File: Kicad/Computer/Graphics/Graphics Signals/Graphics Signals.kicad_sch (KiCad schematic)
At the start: 26 parts, among them IC1 74LVC1G04GV,125, IC10 74LVC74APW,118, IC11 74LVC32APW,118, IC2 74LVC74APW,118, IC2 AP7365-33WG-7, IC3 74LVC74APW,118, IC4 SN74LVC1G332DCKR, IC6 74LVC125APW-Q100J, IC9 74LVC1GX04GW,125, J7 Conn_02x16_Counter_Clockwise

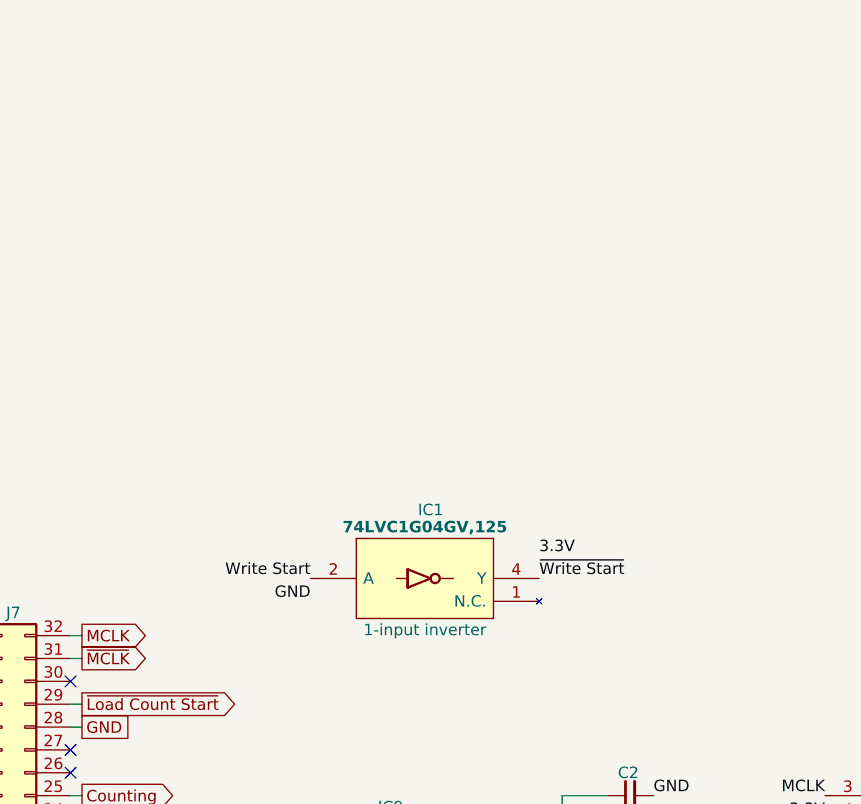
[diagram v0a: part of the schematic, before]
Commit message: Added a Blitter Board.
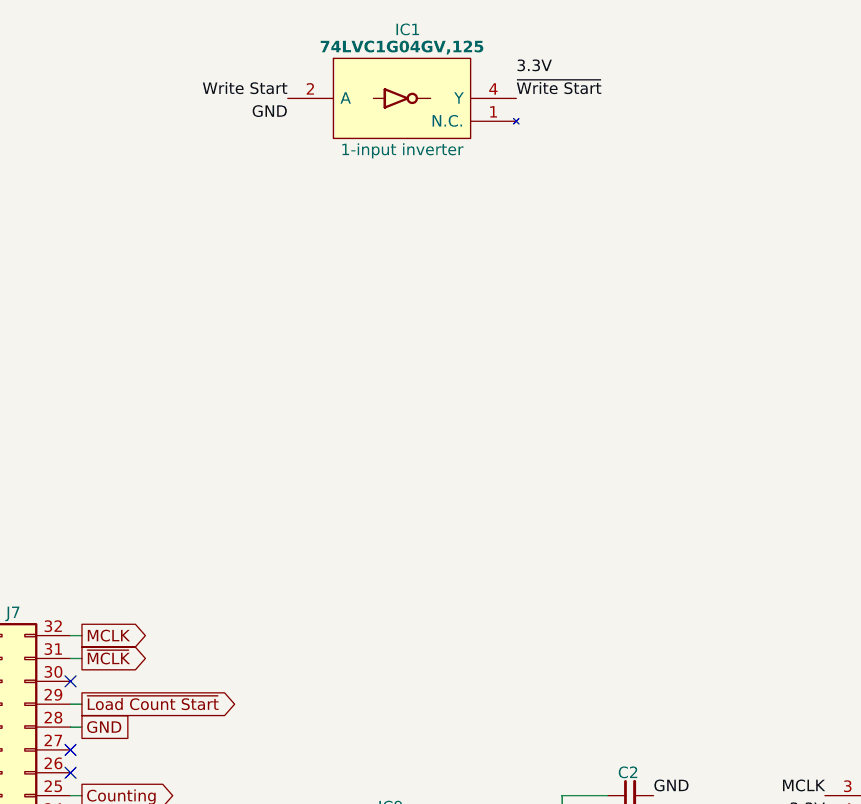
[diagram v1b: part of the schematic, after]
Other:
- moved on the sheet: IC1
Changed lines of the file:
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@@
 	)
 	(label "~{Write Start}"
-		(at 97.79 81.28 0)
+		(at 95.25 27.94 0)
 		(fields_autoplaced yes)
 		(effects
@@
 	)
 	(label "GND"
-		(at 72.39 83.82 180)
+		(at 69.85 30.48 180)
 		(fields_autoplaced yes)
 		(effects
@@
 	)
 	(label "Write Start"
-		(at 72.39 81.28 180)
+		(at 69.85 27.94 180)
 		(fields_autoplaced yes)
 		(effects
@@
 	)
 	(label "3.3V"
-		(at 97.79 78.74 0)
+		(at 95.25 25.4 0)
 		(fields_autoplaced yes)
 		(effects
@@
 	(symbol
 		(lib_id "Nexperia:74LVC1G04GV,125")
-		(at 72.39 78.74 0)
+		(at 69.85 25.4 0)
 		(unit 1)
 		(exclude_from_sim no)
@@
 		(dnp no)
 		(property "Reference" "IC1"
-			(at 85.725 73.66 0)
+			(at 83.185 20.32 0)
 			(effects
 				(font
@@
 		)
 		(property "Value" "74LVC1G04GV,125"
-			(at 85.09 75.565 0)
+			(at 82.55 22.225 0)
 			(effects
 				(font
@@
 		)
 		(property "Footprint" "SamacSys_Parts:SOT95P275X110-5N"
-			(at 98.425 101.6 0)
+			(at 95.885 48.26 0)
 			(effects
 				(font
@@
 		)
 		(property "Datasheet" "https://assets.nexperia.com/documents/data-sheet/74LVC1G04.pdf"
-			(at 98.425 104.14 0)
+			(at 95.885 50.8 0)
 			(effects
 				(font
@@
 		)
 		(property "Description" "1-input inverter"
-			(at 85.09 86.995 0)
+			(at 82.55 33.655 0)
 			(effects
 				(font
@@
 		)
 		(property "Height" "1.1"
-			(at 98.425 109.22 0)
+			(at 95.885 55.88 0)
 			(effects
 				(font
@@
 		)
 		(property "Manufacturer_Name" "Nexperia"
-			(at 98.425 111.76 0)
+			(at 95.885 58.42 0)
 			(effects
 				(font
@@
 		)
 		(property "Manufacturer_Part_Number" "74LVC1G04GV,125"
-			(at 98.425 114.3 0)
+			(at 95.885 60.96 0)
 			(effects
 				(font
@@
 		)
 		(property "Mouser Part Number" "771-74LVC1G04GV"
-			(at 98.425 116.84 0)
+			(at 95.885 63.5 0)
 			(effects
 				(font
@@
 		)
 		(property "Mouser Price/Stock" "https://www.mouser.co.uk/ProductDetail/Nexperia/74LVC1G04GV125?qs=me8TqzrmIYW6McwMAxl%2F9w%3D%3D"
-			(at 98.425 119.38 0)
+			(at 95.885 66.04 0)
 			(effects
 				(font
@@
 		)
 		(property "Silkscreen" "'1G04"
-			(at 85.725 89.535 0)
-			(effects
-				(font
+			(at 83.185 36.195 0)
+			(effects
+				(font

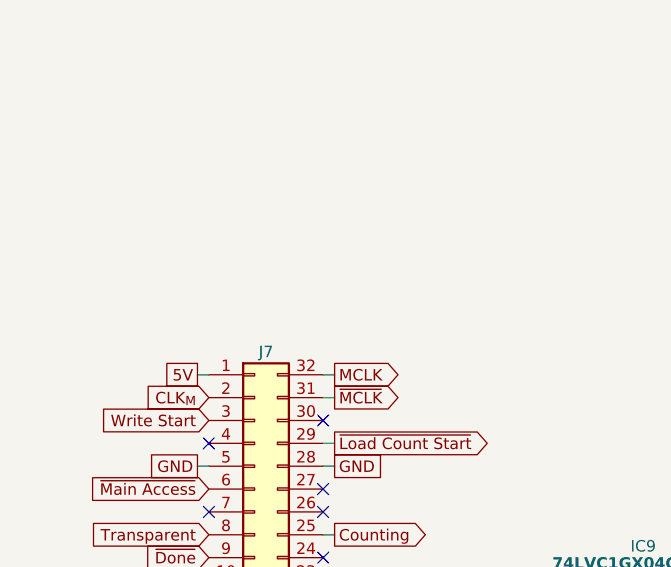
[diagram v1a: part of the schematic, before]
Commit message: Use VRML instead of STEPs for Processor Board models.
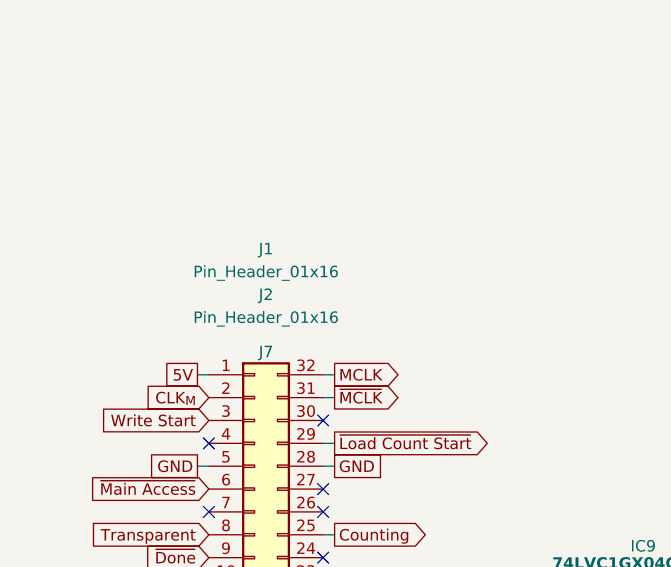
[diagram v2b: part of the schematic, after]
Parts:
- added J1, J2: Pin_Header_01x16, SamacSys_Parts:PinHeader_1x16_P2.54mm_Vertical, symbol HCP65:Pin_Header_01x32
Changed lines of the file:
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@@
+	)
+	(symbol
+		(lib_id "HCP65:Pin_Header_01x32")
+		(at 39.37 74.93 0)
+		(mirror y)
+		(unit 1)
+		(exclude_from_sim no)
+		(in_bom yes)
+		(on_board yes)
+		(dnp no)
+		(property "Reference" "J1"
+			(at 39.37 73.66 0)
+			(effects
+				(font
+					(size 1.27 1.27)
+				)
+			)
+		)
+		(property "Value" "Pin_Header_01x16"
+			(at 39.37 76.2 0)
+			(effects
+				(font
+					(size 1.27 1.27)
+				)
+			)
+		)
+		(property "Footprint" "SamacSys_Parts:PinHeader_1x16_P2.54mm_Vertical"
+			(at 39.37 78.74 0)
+			(effects
+				(font
+					(size 1.27 1.27)
+				)
+				(hide yes)
+			)
+		)
+		(property "Datasheet" "~"
+			(at 44.45 74.93 0)
+			(effects
+				(font
+					(size 1.27 1.27)
+				)
+				(hide yes)
+			)
+		)
+		(property "Description" ""
+			(at 39.37 74.93 0)
+			(effects
+				(font
+					(size 1.27 1.27)
+				)
+				(hide yes)
+			)
+		)
+		(instances
+			(project "Graphics Signals"
+				(path "/5ce90b85-49a2-4937-86c7-662b0d6f8431"
+					(reference "J1")
+					(unit 1)
+				)
+			)
+		)
 	)
 	(symbol
@@
 					(unit 1)
 				)
+			)
+		)
+	)
+	(symbol
+		(lib_id "HCP65:Pin_Header_01x32")
+		(at 39.37 80.01 0)
+		(unit 1)
+		(exclude_from_sim no)
+		(in_bom yes)
+		(on_board yes)
+		(dnp no)
+		(property "Reference" "J2"
+			(at 39.37 78.74 0)
+			(effects
+				(font
+					(size 1.27 1.27)
+				)
+			)
+		)
+		(property "Value" "Pin_Header_01x16"
+			(at 39.37 81.28 0)
+			(effects
+				(font
+					(size 1.27 1.27)
+				)
+			)
+		)
+		(property "Footprint" "SamacSys_Parts:PinHeader_1x16_P2.54mm_Vertical"
+			(at 39.37 83.82 0)
+			(effects
+				(font
+					(size 1.27 1.27)
+				)
+				(hide yes)
+			)
+		)
+		(property "Datasheet" "~"
+			(at 34.29 80.01 0)
+			(effects
+				(font
+					(size 1.27 1.27)
+				)
+				(hide yes)
+			)
+		)
+		(property "Description" ""
+			(at 39.37 80.01 0)
+			(effects
+				(font
+					(size 1.27 1.27)
+				)
+				(hide yes)
+			)
+		)
+		(instances
+			(project "Graphics Signals"
+				(path "/5ce90b85-49a2-4937-86c7-662b0d6f8431"
+					(reference "J2")
+					(unit 1)
+				)

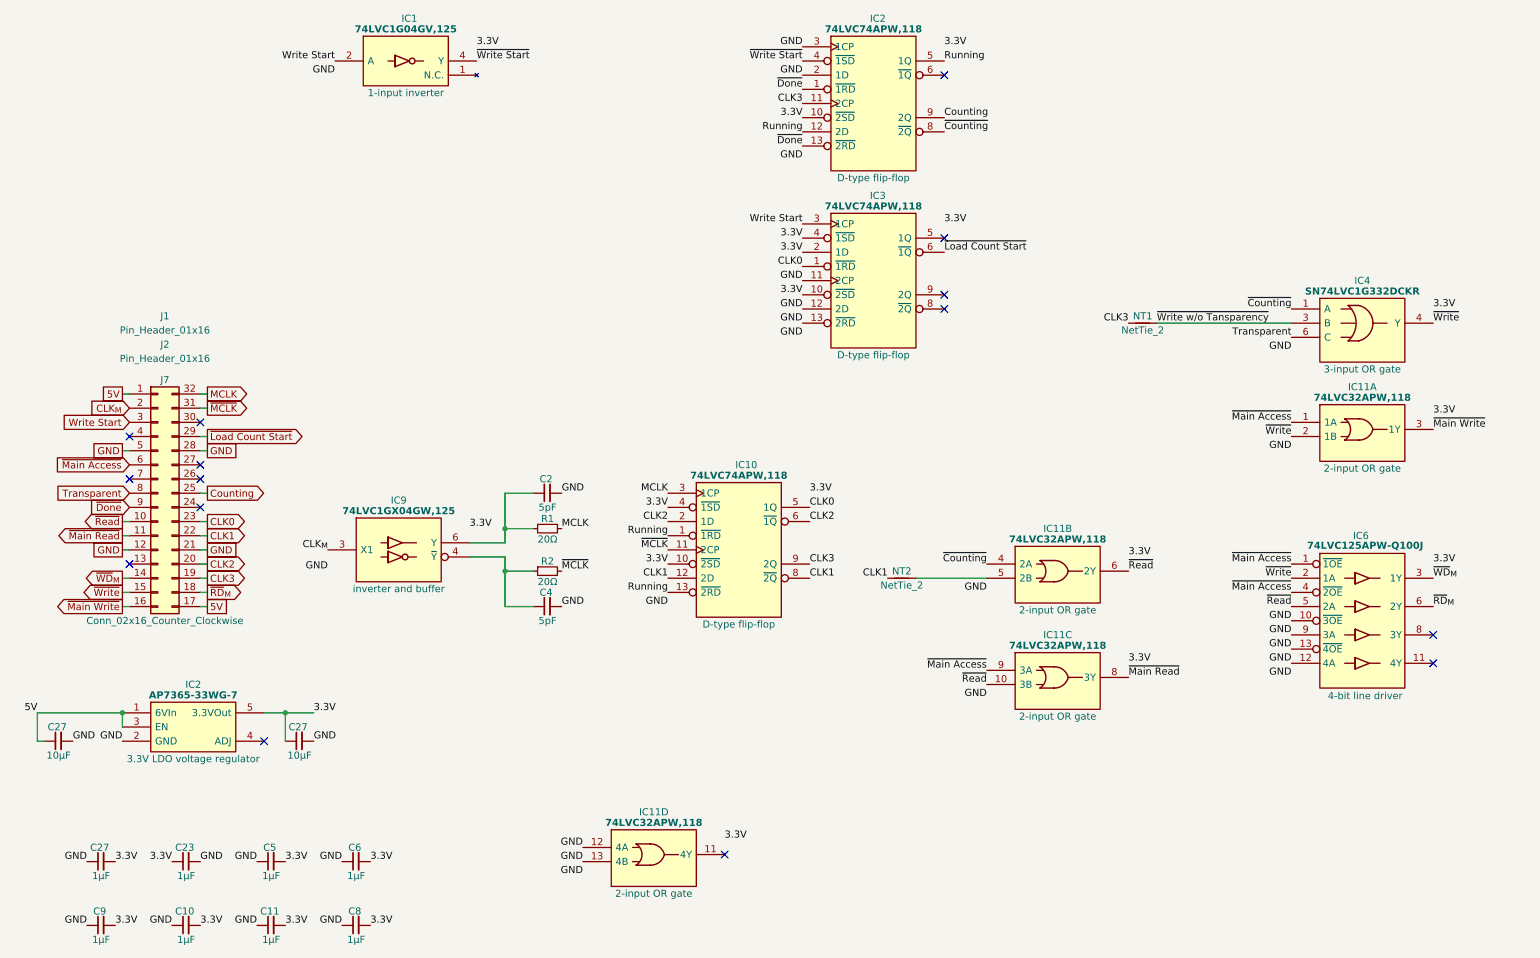
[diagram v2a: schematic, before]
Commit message: Upgraded LCD Board to Kicad 9.0.
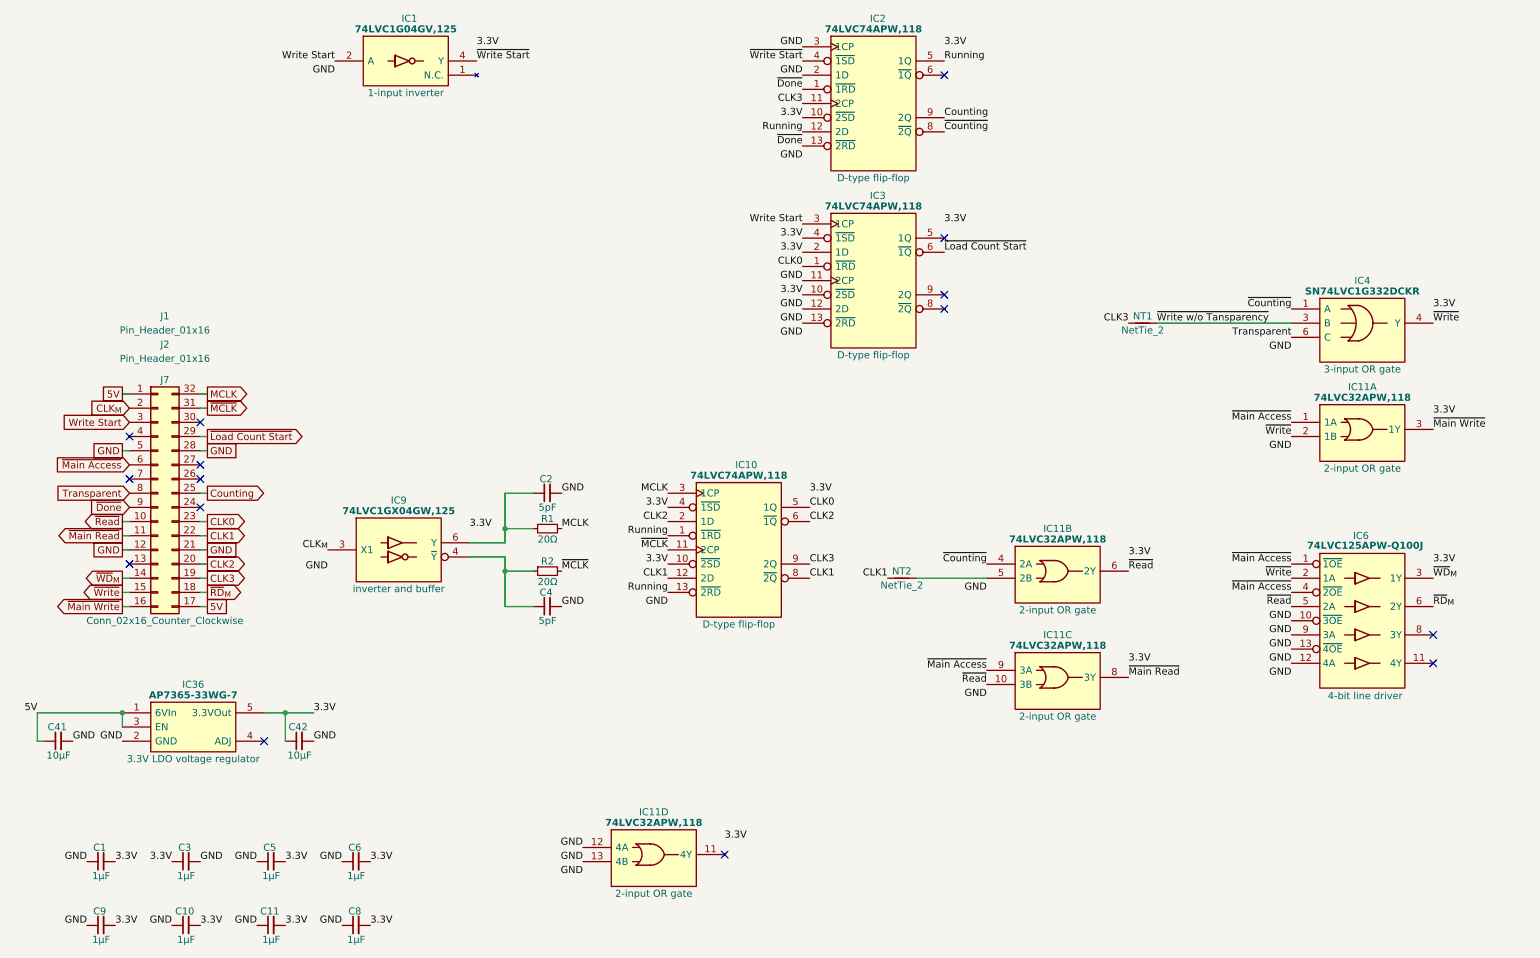
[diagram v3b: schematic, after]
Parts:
- renumbered C27 to C1, C23 to C3, C27 to C41, C27 to C42, IC2 to IC36
